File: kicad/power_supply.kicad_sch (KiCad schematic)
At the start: 17 parts, among them J6 Conn_01x02, U5 TPSM53602RDA, U6 TPS62162DSG

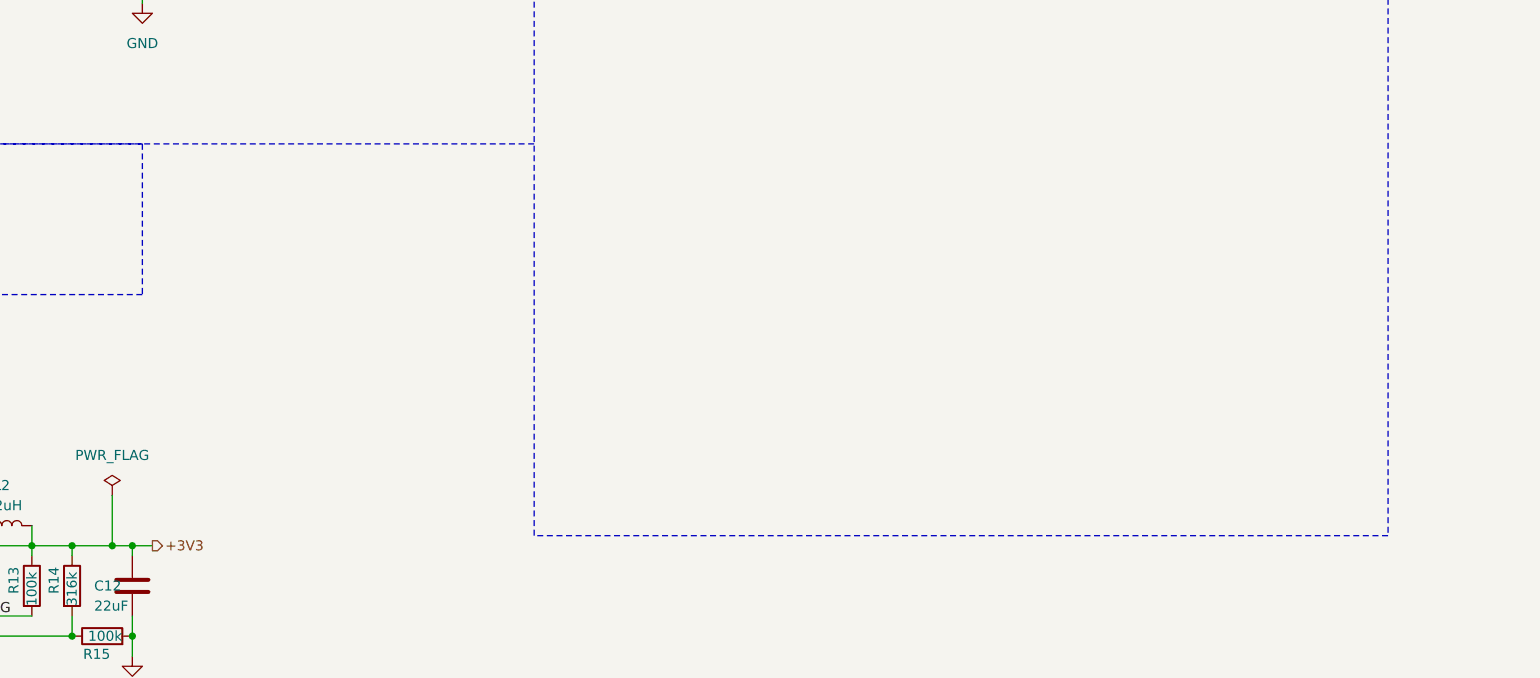
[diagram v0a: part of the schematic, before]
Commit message: docs: update component description for TPS62162DSG
Signed-off-by: Bobo Bäck Engström <bobo@id8-engineering.io>
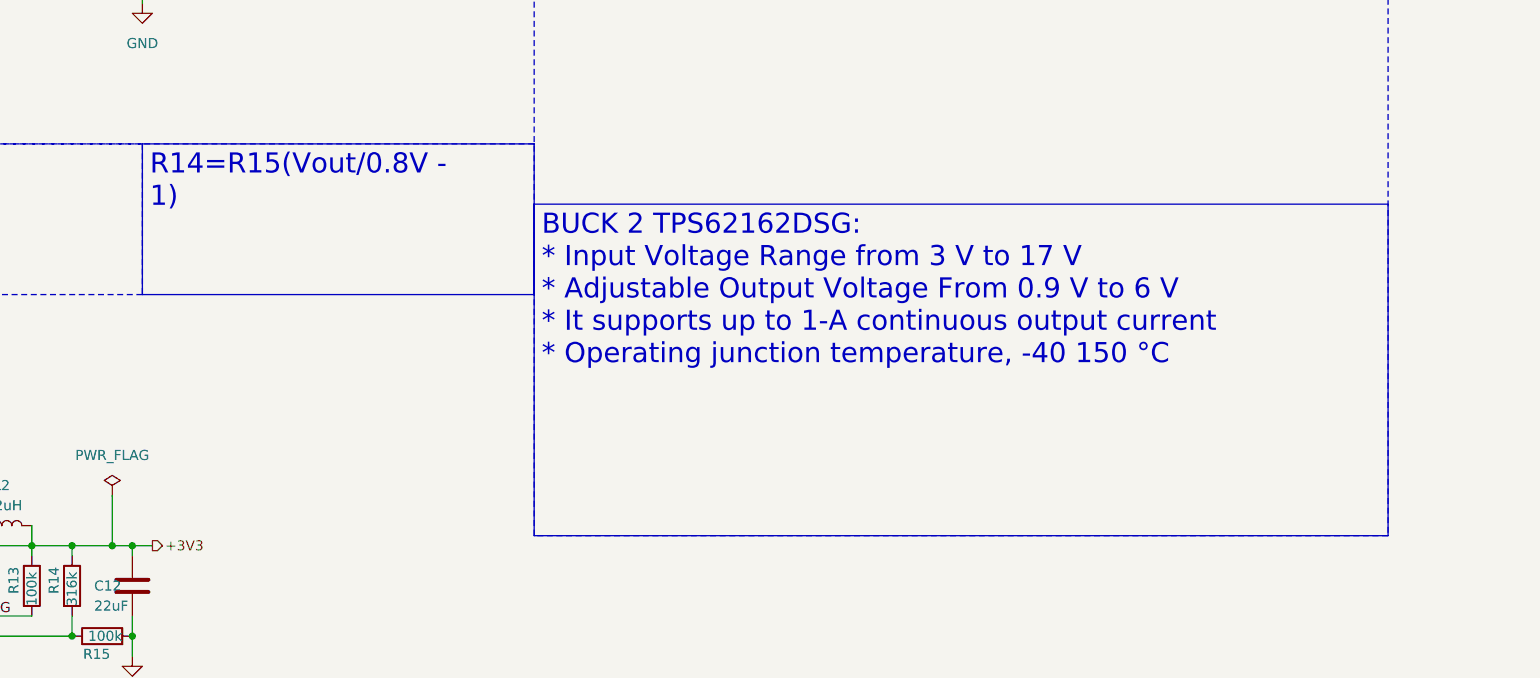
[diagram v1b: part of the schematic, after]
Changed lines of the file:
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@@
+		)
+	)
+	(text_box "R14=R15(Vout/0.8V - 1)"
+		(exclude_from_sim no)
+		(at 127 115.57 0)
+		(size 49.53 19.05)
+		(margins 0.9525 0.9525 0.9525 0.9525)
+		(stroke
+			(width 0)
+			(type solid)
+		)
+		(fill
+			(type none)
+		)
+		(effects
+			(font
+				(size 2.54 2.54)
+			)
+			(justify left top)
 		)
 	)
@@
 		)
 	)
+	(text_box "BUCK 2 TPS62162DSG:\n* Input Voltage Range from 3 V to 17 V\n* Adjustable Output Voltage From 0.9 V to 6 V\n* It supports up to 1-A continuous output current\n* Operating junction temperature, -40 150 °C"
+		(exclude_from_sim no)
+		(at 176.53 123.19 0)
+		(size 107.95 41.91)
+		(margins 0.9525 0.9525 0.9525 0.9525)
+		(stroke
+			(width 0)
+			(type solid)
+		)
+		(fill
+			(type none)
+		)
+		(effects
+			(font
+				(size 2.54 2.54)
+			)
+			(justify left top)
+		)
+	)

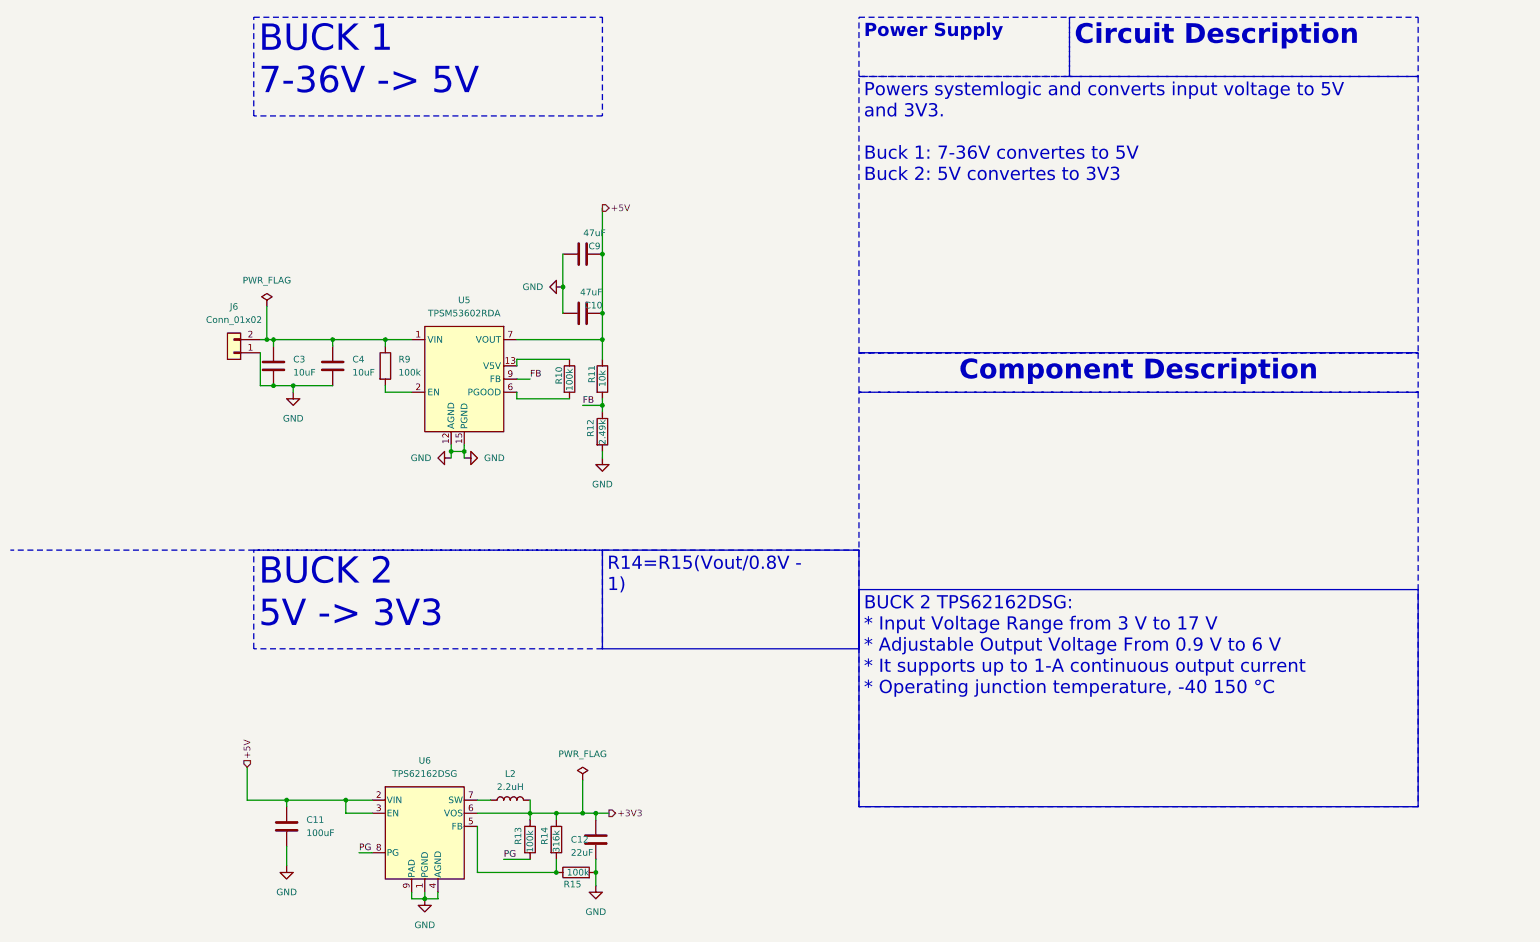
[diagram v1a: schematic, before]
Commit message: feat: remake power management and use the same as the reference DK
Signed-off-by: Bobo Bäck Engström <bobo@id8-engineering.io>
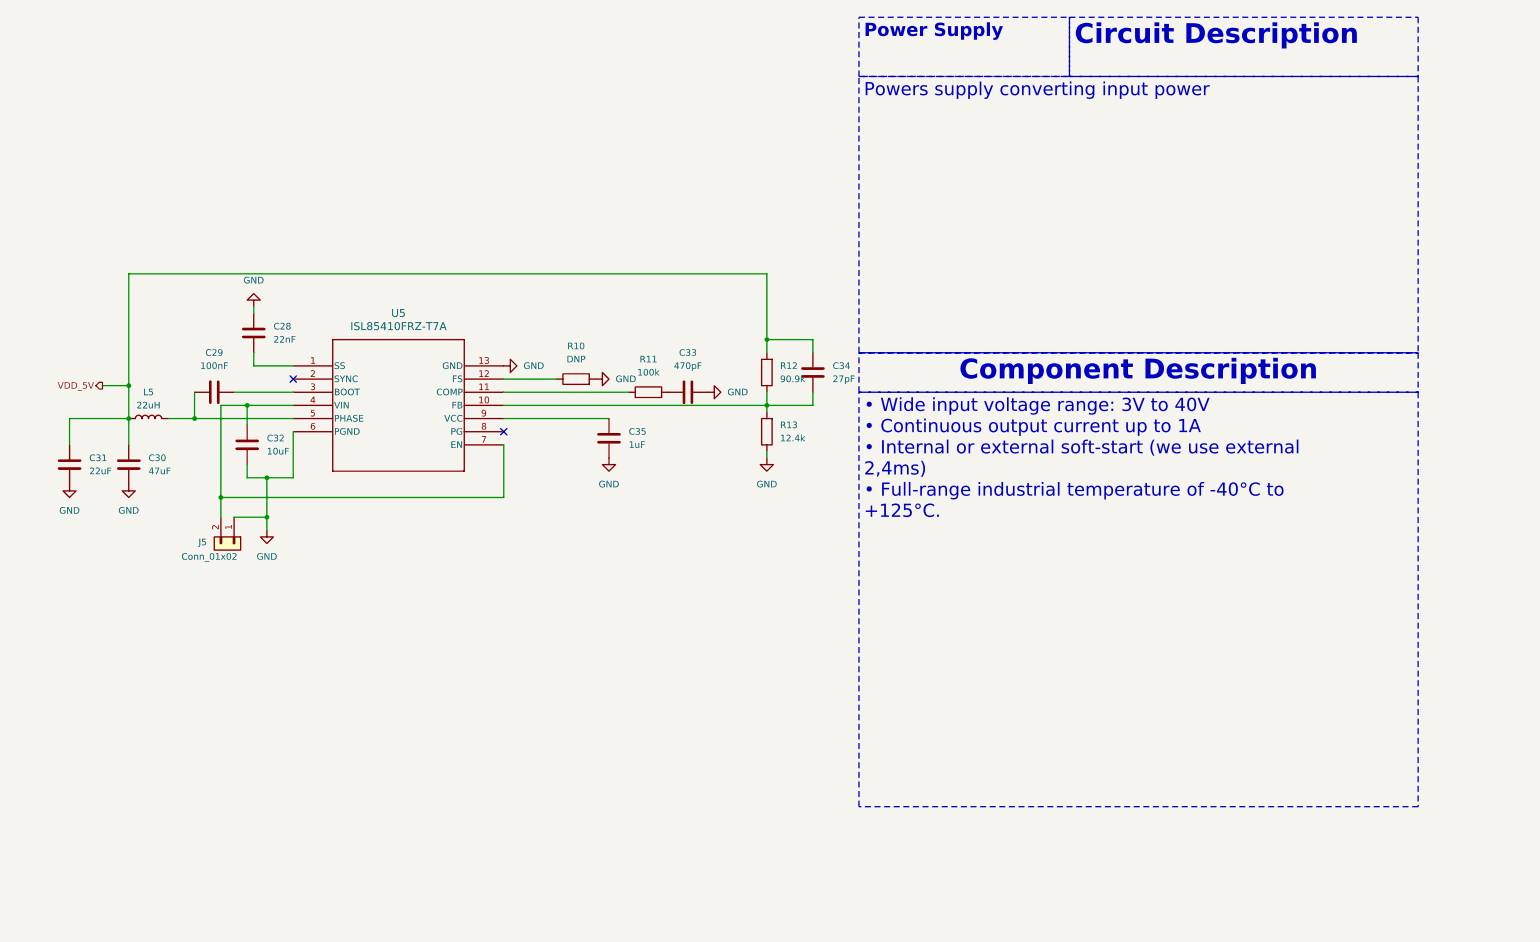
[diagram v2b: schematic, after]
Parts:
- removed C10, C9: 47uF, seven-lib:C_1812_4532Metric, symbol seven_lib:C
- removed C11: 100uF, seven-lib:C_1812_4532Metric, symbol seven_lib:C
- removed C12: 22uF, seven-lib:C_1812_4532Metric, symbol seven_lib:C
- removed C3, C4: 10uF, seven-lib:C_1812_4532Metric, symbol seven_lib:C
- removed J6: Conn_01x02, seven-lib:PhoenixContact_MSTBA_2,5_2-G-5,08_1x02_P5.08mm_Horizontal, symbol seven_lib:Conn_01x02
- removed L2: 2.2uH, seven-lib:L_1008_2520Metric, symbol seven_lib:L
- removed R14: 316k, seven-lib:R_0603_1608Metric, symbol seven_lib:R
- removed R15, R9: 100k, seven-lib:R_0603_1608Metric, symbol seven_lib:R
- removed U5: TPSM53602RDA, seven-lib:Texas_B3QFN-14-1EP_5x5.5mm_P0.65mm_ThermalVia, symbol seven_lib:TPSM53602RDA
- removed U6: TPS62162DSG, seven-lib:WSON-8-1EP_2x2mm_P0.5mm_EP0.9x1.6mm_ThermalVias, symbol seven_lib:TPS62162DSG
- added C28: 22nF, seven-lib:C_1812_4532Metric, symbol seven_lib:C
- added C29: 100nF, seven-lib:C_1812_4532Metric, symbol seven_lib:C
- added C30: 47uF, seven-lib:C_1812_4532Metric, symbol seven_lib:C
- added C31: 22uF, seven-lib:C_1812_4532Metric, symbol seven_lib:C
- added C32: 10uF, seven-lib:C_1812_4532Metric, symbol seven_lib:C
- added C33: 470pF, seven-lib:C_1812_4532Metric, symbol seven_lib:C
- added C34: 27pF, seven-lib:C_1812_4532Metric, symbol seven_lib:C
- added C35: 1uF, seven-lib:C_1812_4532Metric, symbol seven_lib:C
- added J5: Conn_01x02, seven-lib:PhoenixContact_MSTBA_2,5_2-G-5,08_1x02_P5.08mm_Horizontal, symbol seven_lib:Conn_01x02
- added L5: 22uH, seven-lib:L_1008_2520Metric, symbol seven_lib:L
- added U5: ISL85410FRZ-T7A, seven-lib:DFN12_L12.4X3_REN, symbol seven_lib:ISL85410FRZ-T7A
- R10: value 100k -> DNP
- R11: value 10k -> 100k
- R12: value 2.49k -> 90.9k
- R13: value 100k -> 12.4k
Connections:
- net +3V3 is gone; now on net GND: R13.1
- net PG is gone; now on an unnamed net: R13.2
- net GND: now also R10.2, C28.2, C30.2, C31.2, C32.2, C33.1, C35.1, J5.1 (GND), U5.13 (GND), U5.6 (PGND); no longer R12.2
- net at R10.1: now also U5.12 (FS)
- net +5V: no longer names the net of R11.1
- net +5V: now also U5.11 (COMP)
- net FB: no longer names the net of R12.1
- net FB: now also C34.2, U5.10 (FB); no longer R11.2
- new net: C28.1, U5.1 (SS)
- new net: C29.1, U5.3 (BOOT)
- new net: C32.1, J5.2 (VIN), U5.4 (VIN), U5.7 (EN)
- new net: C29.2, L5.2, U5.5 (PHASE)
- new net: C35.2, U5.9 (VCC)
- new net: C33.2, R11.2
- new net VDD_5V: C30.1, C31.1, C34.1, L5.1, R12.2
- no-connect marks 0 -> 2

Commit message: docs: update documentation to be more accurate
Signed-off-by: Bobo Bäck Engström <bobo@id8-engineering.io>
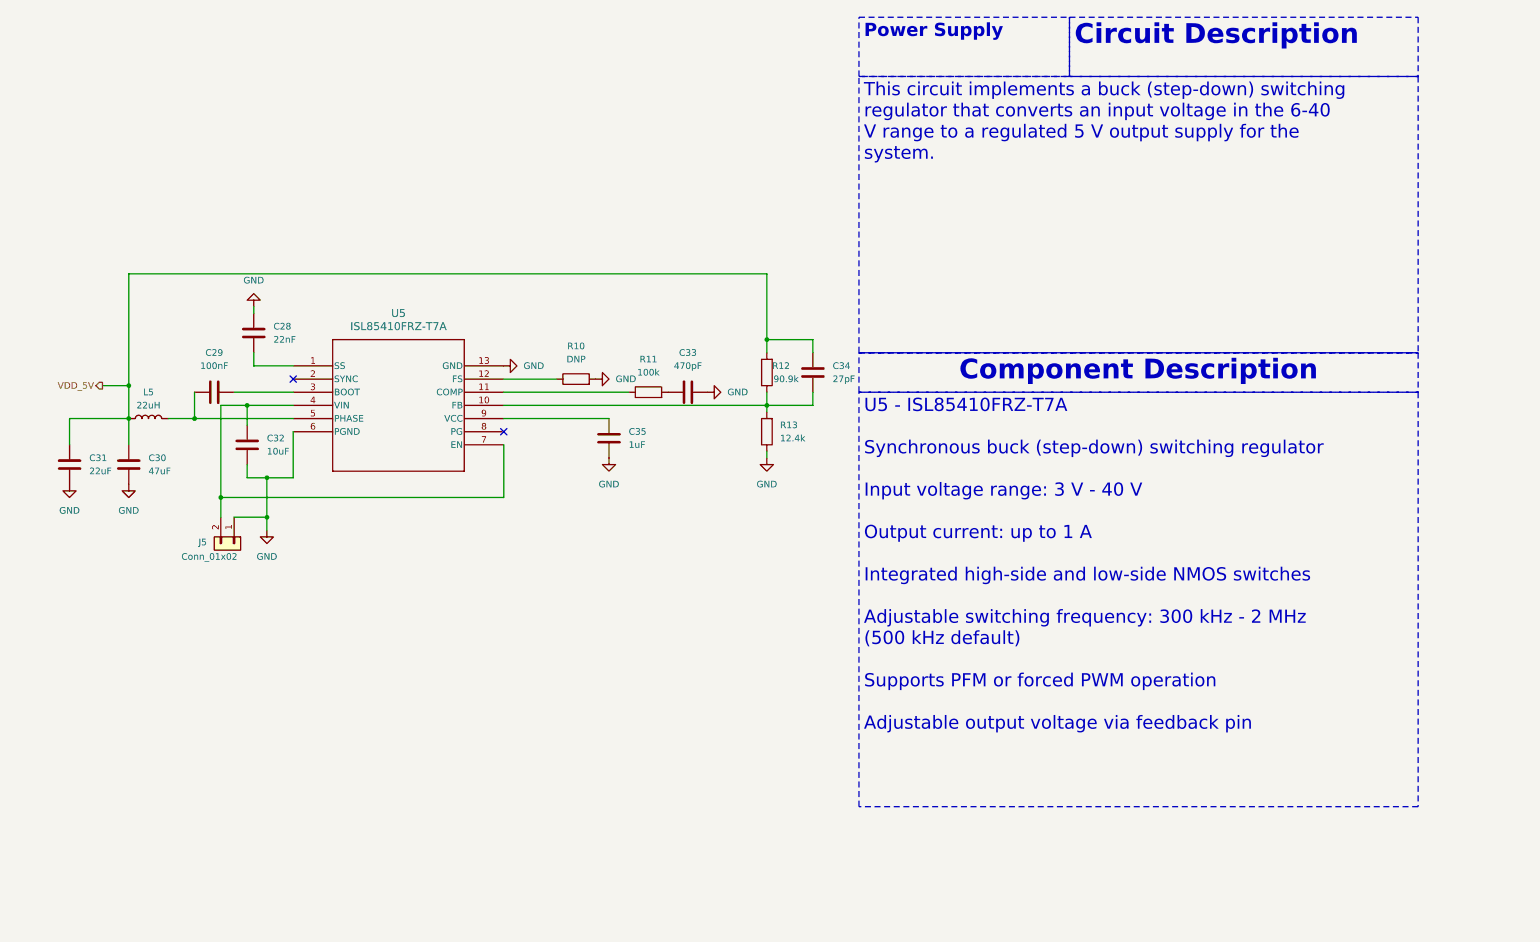
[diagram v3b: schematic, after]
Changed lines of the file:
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@@
 		)
 	)
-	(text_box "• Wide input voltage range: 3V to 40V\n• Continuous output current up to 1A\n• Internal or external soft-start (we use external 2,4ms)\n• Full-range industrial temperature of -40°C to +125°C."
+	(text_box "U5 - ISL85410FRZ-T7A\n\nSynchronous buck (step-down) switching regulator\n\nInput voltage range: 3 V - 40 V\n\nOutput current: up to 1 A\n\nIntegrated high-side and low-side NMOS switches\n\nAdjustable switching frequency: 300 kHz - 2 MHz (500 kHz default)\n\nSupports PFM or forced PWM operation\n\nAdjustable output voltage via feedback pin"
 		(exclude_from_sim no)
 		(at 176.53 85.09 0)
@@
 		)
 	)
-	(text_box "Powers supply converting input power\n"
+	(text_box "This circuit implements a buck (step-down) switching regulator that converts an input voltage in the 6-40 V range to a regulated 5 V output supply for the system."
 		(exclude_from_sim no)
 		(at 176.53 24.13 0)
@@
 			)
 		)
-		(property "Datasheet" "ISL85410FRZ-T7A"
+		(property "Datasheet" "https://eu.mouser.com/datasheet/3/1166/1/REN_isl854102_DST_20131109.pdf"
 			(at 67.31 80.01 0)
 			(effects
@@
 		(on_board yes)
 		(dnp no)
-		(fields_autoplaced yes)
 		(property "Reference" "R12"
-			(at 161.29 80.0099 0)
+			(at 159.766 80.01 0)
 			(effects
 				(font
@@
 		)
 		(property "Value" "90.9k"
-			(at 161.29 82.5499 0)
-			(effects
-				(font
+			(at 160.02 82.55 0)
+			(effects
+				(font

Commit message: fix: change C fp to smaller one.
Signed-off-by: Bobo Bäck Engström <bobo@id8-engineering.io>
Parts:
- C28, C29, C30, C31, C32, C33, C34, C35: footprint seven-lib:C_1812_4532Metric -> seven-lib:C_0402_1005Metric
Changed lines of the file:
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@@
 			)
 		)
-		(property "Footprint" "seven-lib:C_1812_4532Metric"
+		(property "Footprint" "seven-lib:C_0402_1005Metric"
 			(at 58.7248 69.85 0)
 			(effects
@@
 			)
 		)
-		(property "Footprint" "seven-lib:C_1812_4532Metric"
+		(property "Footprint" "seven-lib:C_0402_1005Metric"
 			(at 25.0952 102.87 0)
 			(effects
@@
 			)
 		)
-		(property "Footprint" "seven-lib:C_1812_4532Metric"
+		(property "Footprint" "seven-lib:C_0402_1005Metric"
 			(at 139.7 86.0552 0)
 			(effects
@@
 			)
 		)
-		(property "Footprint" "seven-lib:C_1812_4532Metric"
+		(property "Footprint" "seven-lib:C_0402_1005Metric"
 			(at 127.3048 90.17 0)
 			(effects
@@
 			)
 		)
-		(property "Footprint" "seven-lib:C_1812_4532Metric"
+		(property "Footprint" "seven-lib:C_0402_1005Metric"
 			(at 168.6052 85.09 0)
 			(effects
@@
 			)
 		)
-		(property "Footprint" "seven-lib:C_1812_4532Metric"
+		(property "Footprint" "seven-lib:C_0402_1005Metric"
 			(at 48.26 86.0552 0)
 			(effects
@@
 			)
 		)
-		(property "Footprint" "seven-lib:C_1812_4532Metric"
+		(property "Footprint" "seven-lib:C_0402_1005Metric"
 			(at 59.3852 99.06 0)
 			(effects
@@
 			)
 		)
-		(property "Footprint" "seven-lib:C_1812_4532Metric"
+		(property "Footprint" "seven-lib:C_0402_1005Metric"
 			(at 36.5252 102.87 0)
 			(effects

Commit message: fix: change R fp to a smaller one
Signed-off-by: Bobo Bäck Engström <bobo@id8-engineering.io>
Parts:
- L5: footprint seven-lib:L_1008_2520Metric -> seven-lib:L_0603_1608Metric
- R10, R11, R12, R13: footprint seven-lib:R_0603_1608Metric -> seven-lib:R_0402_1005Metric
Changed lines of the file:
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@@
 			)
 		)
-		(property "Footprint" "seven-lib:R_0603_1608Metric"
+		(property "Footprint" "seven-lib:R_0402_1005Metric"
 			(at 135.89 86.868 90)
 			(effects
@@
 			)
 		)
-		(property "Footprint" "seven-lib:R_0603_1608Metric"
+		(property "Footprint" "seven-lib:R_0402_1005Metric"
 			(at 121.92 84.328 90)
 			(effects
@@
 			)
 		)
-		(property "Footprint" "seven-lib:R_0603_1608Metric"
+		(property "Footprint" "seven-lib:R_0402_1005Metric"
 			(at 160.528 81.28 90)
 			(effects
@@
 			)
 		)
-		(property "Footprint" "seven-lib:L_1008_2520Metric"
+		(property "Footprint" "seven-lib:L_0603_1608Metric"
 			(at 39.37 90.17 0)
 			(effects
@@
 			)
 		)
-		(property "Footprint" "seven-lib:R_0603_1608Metric"
+		(property "Footprint" "seven-lib:R_0402_1005Metric"
 			(at 160.528 92.71 90)
 			(effects

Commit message: fix: changes made according to review meeting
Signed-off-by: Bobo Bäck Engström <bobo@id8-engineering.io>
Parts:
- added TP6: VDD_5V, seven-lib:TestPoint_Pad_2.0x2.0mm, symbol seven_lib:TestPoint
- added TP7: POWER_SUPPLY, seven-lib:TestPoint_Pad_2.0x2.0mm, symbol seven_lib:TestPoint
- added TP8: FB, seven-lib:TestPoint_Pad_2.0x2.0mm, symbol seven_lib:TestPoint
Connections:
- net VDD_5V: now also TP6.1
- net at C34.2, R12.1, R13.2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: now also TP8.1
- net at C32.1, J5.2 (VIN), U5.4 (VIN)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: now also TP7.1
